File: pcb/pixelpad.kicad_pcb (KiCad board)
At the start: 2 copper layers, 61.5 x 55.5 mm, 17 parts, among them J1 OLED Display, SW1 SW_Push_45deg, SW2 SW_Push_45deg, SW3 RotaryEncoder_Switch, SW4 SW_Push_45deg, SW5 SW_Push_45deg, SW6 SW_Push_45deg, U1 MOUDLE-SEEEDUINO-XIAO

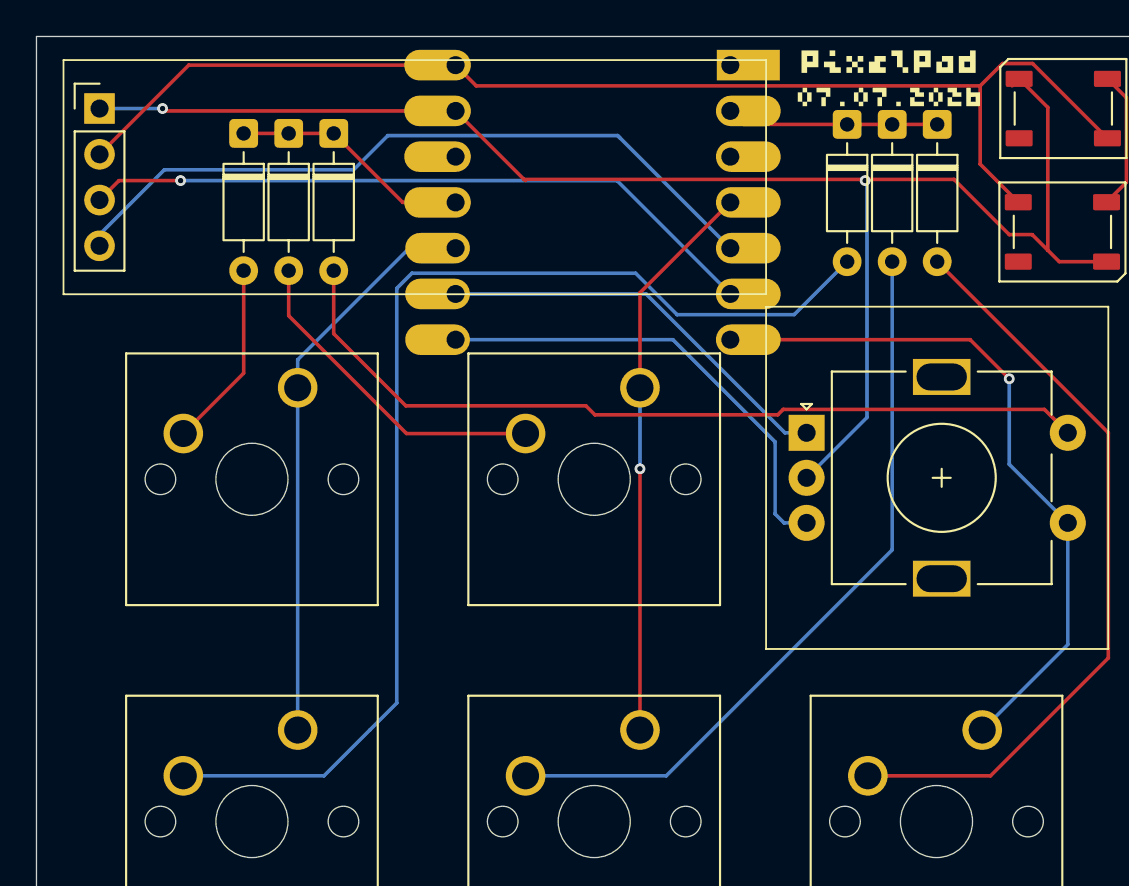
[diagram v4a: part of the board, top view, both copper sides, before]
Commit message: Ran the Cleanup Tracks and Vias
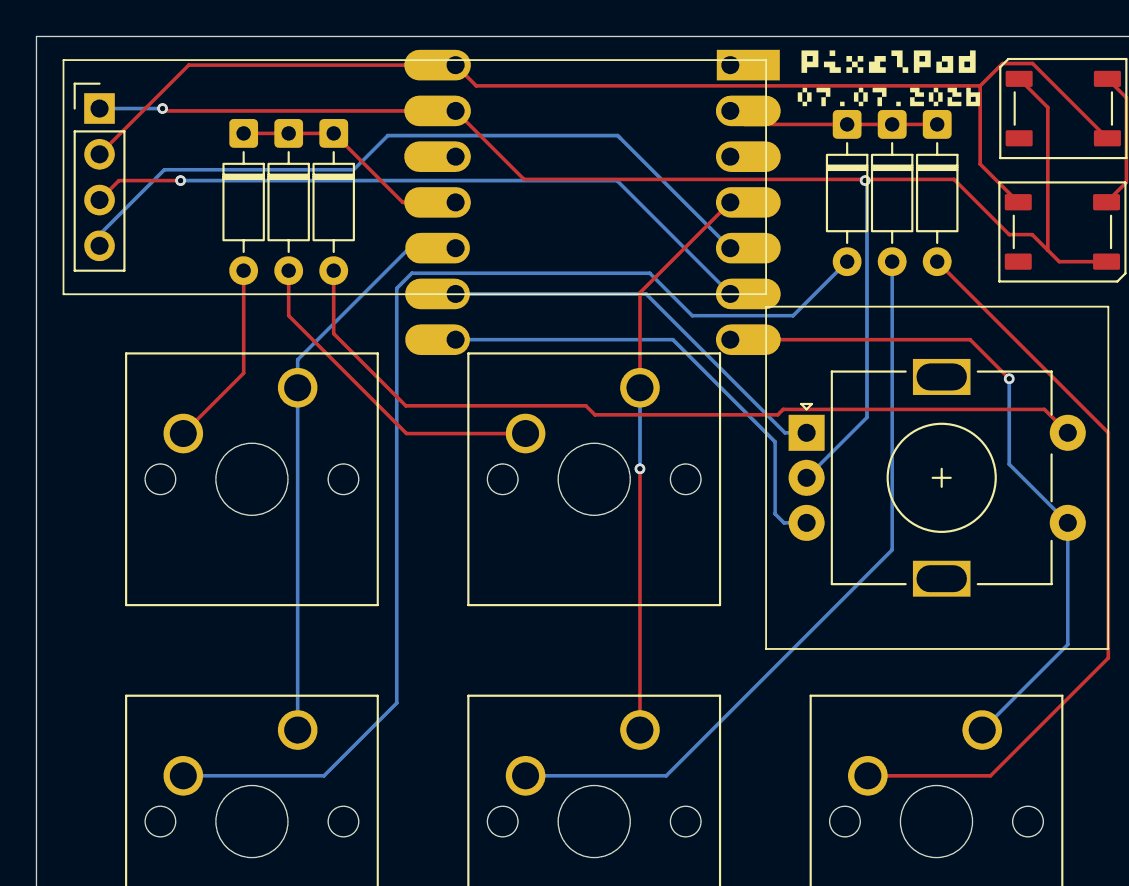
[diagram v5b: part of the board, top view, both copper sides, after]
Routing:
- net COL0: track 31.9 -> 29.3 mm
- net ROW1: track 11.8 -> 10.7 mm
- net GND: track 88.2 -> 87.5 mm
- net SDA: track 40.6 -> 40.0 mm
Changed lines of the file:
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@@
-	)
-	(segment
-		(start 82.566243 42.433757)
-		(end 82.632485 42.5)
-		(width 0.2)
-		(layer "F.Cu")
-		(net "GND")
 	)
 	(segment
@@
 		(start 110.774999 45.5)
 		(end 111.6375 46.3625)
-		(width 0.2)
-		(layer "F.Cu")
-		(net "GND")
-	)
-	(segment
-		(start 109.657985 37.242015)
-		(end 110.05 36.85)
 		(width 0.2)
 		(layer "F.Cu")
@@
 	)
 	(segment
-		(start 94.0145 38.632015)
-		(end 94.762485 39.38)
-		(width 0.2)
-		(layer "F.Cu")
-		(net "ROW1")
-	)
-	(segment
 		(start 103 39.38)
 		(end 105.5 39.38)
@@
 	)
 	(segment
+		(start 75.5 71.5)
+		(end 71.46 75.54)
+		(width 0.2)
+		(layer "B.Cu")
+		(net "Net-(D6-A)")
+	)
+	(segment
+		(start 76.338154 47.642015)
+		(end 75.5 48.480169)
+		(width 0.2)
+		(layer "B.Cu")
+		(net "Net-(D6-A)")
+	)
+	(segment
 		(start 100.5 47)
-		(end 97.557985 49.942015)
-		(width 0.2)
-		(layer "B.Cu")
-		(net "Net-(D6-A)")
-	)
-	(segment
-		(start 91.057701 49.942015)
-		(end 88.757701 47.642015)
-		(width 0.2)
-		(layer "B.Cu")
-		(net "Net-(D6-A)")
-	)
-	(segment
-		(start 74 73)
-		(end 71.46 75.54)
-		(width 0.2)
-		(layer "B.Cu")
-		(net "Net-(D6-A)")
-	)
-	(segment
-		(start 75.5 71.5)
-		(end 74 73)
-		(width 0.2)
-		(layer "B.Cu")
-		(net "Net-(D6-A)")
-	)
-	(segment
-		(start 97.557985 49.942015)
-		(end 91.057701 49.942015)
-		(width 0.2)
-		(layer "B.Cu")
-		(net "Net-(D6-A)")
-	)
-	(segment
-		(start 88.757701 47.642015)
+		(end 97.5 50)
+		(width 0.2)
+		(layer "B.Cu")
+		(net "Net-(D6-A)")
+	)
+	(segment
+		(start 97.5 50)
+		(end 91.903921 50)
+		(width 0.2)
+		(layer "B.Cu")
+		(net "Net-(D6-A)")
+	)
+	(segment
+		(start 91.903921 50)
+		(end 89.545936 47.642015)
+		(width 0.2)
+		(layer "B.Cu")
+		(net "Net-(D6-A)")
+	)
+	(segment
+		(start 89.545936 47.642015)
 		(end 76.338154 47.642015)
+		(width 0.2)
+		(layer "B.Cu")
+		(net "Net-(D6-A)")
+	)
+	(segment
+		(start 71.46 75.54)
+		(end 63.65 75.54)
 		(width 0.2)
 		(layer "B.Cu")
@@
 	)
 	(segment
-		(start 71.46 75.54)
-		(end 63.65 75.54)
-		(width 0.2)
-		(layer "B.Cu")
-		(net "Net-(D6-A)")
-	)
-	(segment
-		(start 76.338154 47.642015)
-		(end 75.5 48.480169)
-		(width 0.2)
-		(layer "B.Cu")
-		(net "Net-(D6-A)")
-	)
-	(segment
 		(start 76.192351 46.252015)
 		(end 70 52.444366)
-		(width 0.2)
-		(layer "B.Cu")
-		(net "COL0")
-	)
-	(segment
-		(start 78.7645 46.252015)
-		(end 76.192351 46.252015)
 		(width 0.2)
 		(layer "B.Cu")
@@
 	)
 	(segment
-		(start 59 45.5)
-		(end 59 46.12)
-		(width 0.2)
-		(layer "B.Cu")
-		(net "SDA")
-	)
-	(segment

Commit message: Fixed the led schematic and footprint to the right one
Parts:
- D1, D2: footprint LED_SMD:LED_WS2812B_PLCC4_5.0x5.0mm_P3.2mm -> XIAO:SK6812MINI-E_fixed
- moved D1 0.45 mm to (112.0, 38.5)
- moved D2 0.45 mm to (112.0, 45.4)
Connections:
- U1 pad 3: unconnected-(U1-PA10_A2_D2-Pad3) -> WS281B
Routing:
- net WS281B: track 0.00 -> 16.9 mm, vias 0 -> 1
- net VCC: track 68.0 -> 65.5 mm, vias 0 -> 1
- net GND: track 87.5 -> 86.3 mm
- net Net-(D1-DOUT): track 7.74 -> 8.25 mm
